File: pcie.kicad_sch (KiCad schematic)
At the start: 1 part, among them U1 MPFS250T-FCVG484

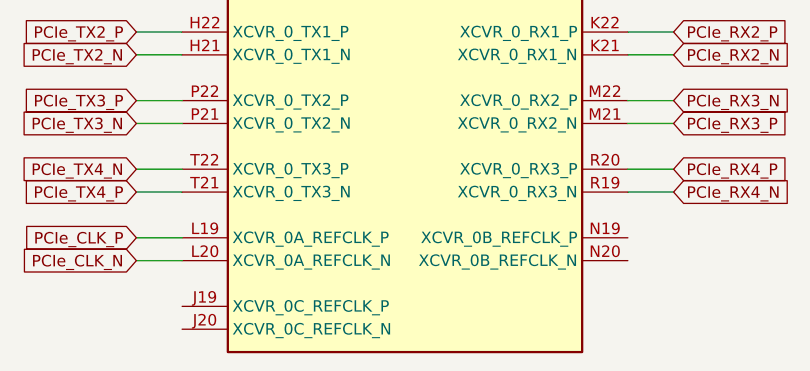
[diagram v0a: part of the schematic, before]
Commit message: [#54899] Flag not connected pins
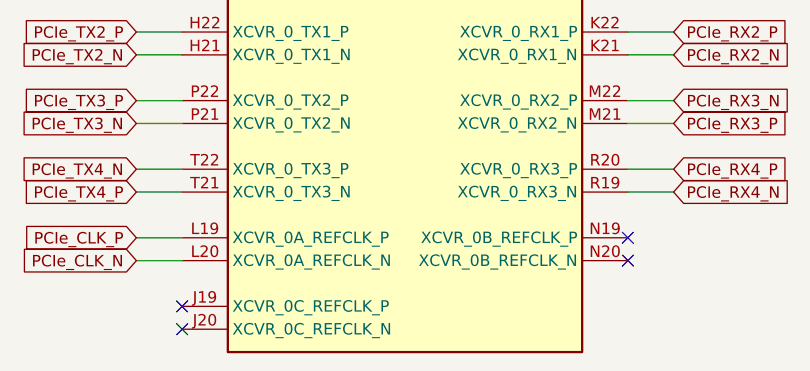
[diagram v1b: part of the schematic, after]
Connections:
- no-connect marks 0 -> 4
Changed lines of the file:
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@@
     (comment 1 "www.antmicro.com")
   )
+  (no_connect (at 177.8 158.75))
+  (no_connect (at 177.8 156.21))
+  (no_connect (at 227.33 148.59))
+  (no_connect (at 227.33 151.13))
   (wire (pts (xy 227.33 125.73) (xy 232.41 125.73))
     (stroke (width 0) (type default))

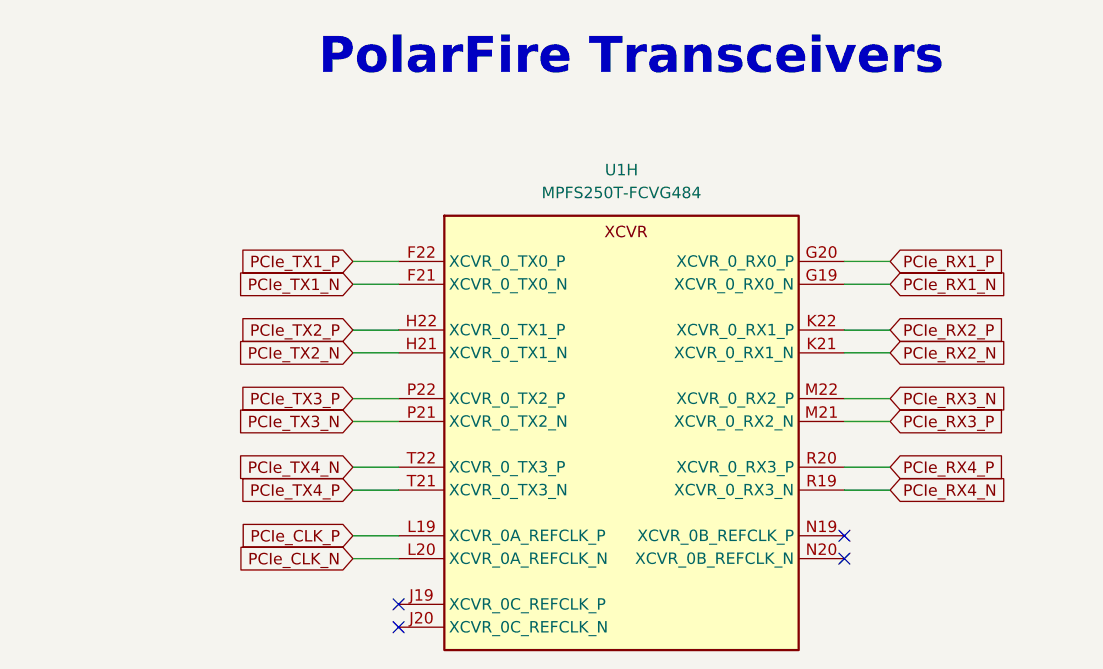
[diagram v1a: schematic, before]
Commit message: [#54899] Rename PCIe connections
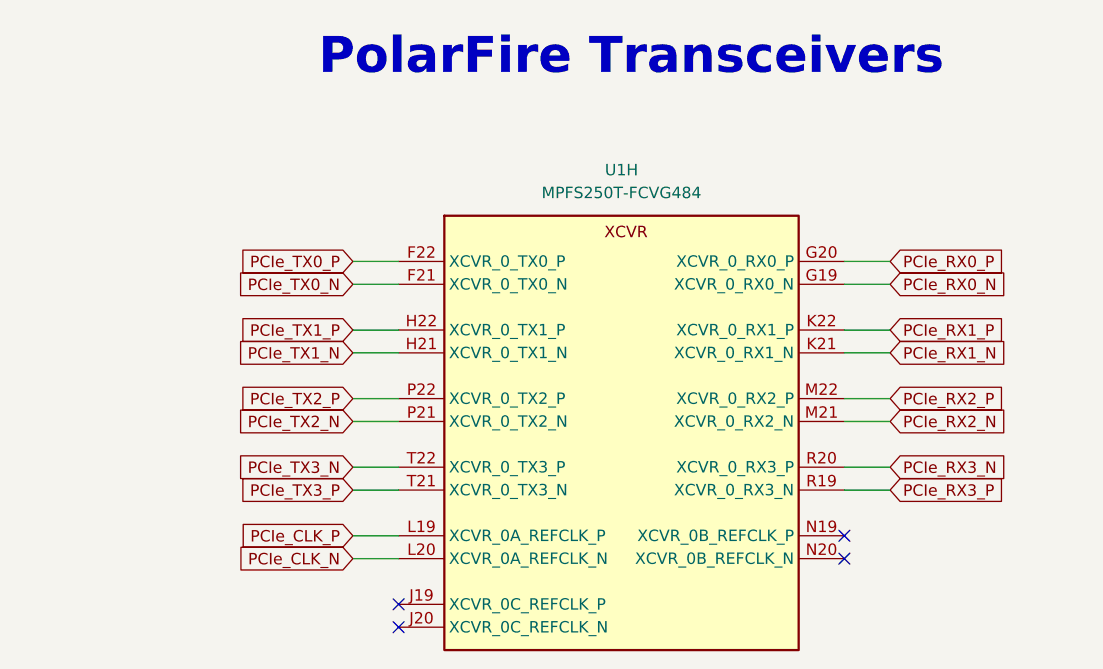
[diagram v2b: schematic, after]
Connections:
- net PCIe_RX4_N is gone; now on net PCIe_RX3_P: U1.R19 (XCVR_0_RX3_N)
- net PCIe_RX4_P is gone; now on net PCIe_RX3_N: U1.R20 (XCVR_0_RX3_P)
- net PCIe_TX4_N is gone; now on net PCIe_TX3_N: U1.T22 (XCVR_0_TX3_P)
- net PCIe_TX4_P is gone; now on net PCIe_TX3_P: U1.T21 (XCVR_0_TX3_N)
- net PCIe_RX1_N: now also U1.K21 (XCVR_0_RX1_N); no longer U1.G19 (XCVR_0_RX0_N)
- net PCIe_RX1_P: now also U1.K22 (XCVR_0_RX1_P); no longer U1.G20 (XCVR_0_RX0_P)
- net PCIe_RX2_N: now also U1.M21 (XCVR_0_RX2_N); no longer U1.K21 (XCVR_0_RX1_N)
- net PCIe_RX2_P: now also U1.M22 (XCVR_0_RX2_P); no longer U1.K22 (XCVR_0_RX1_P)
- net PCIe_RX3_N: no longer U1.M22 (XCVR_0_RX2_P)
- net PCIe_RX3_P: no longer U1.M21 (XCVR_0_RX2_N)
- net PCIe_TX1_N: now also U1.H21 (XCVR_0_TX1_N); no longer U1.F21 (XCVR_0_TX0_N)
- net PCIe_TX1_P: now also U1.H22 (XCVR_0_TX1_P); no longer U1.F22 (XCVR_0_TX0_P)
- net PCIe_TX2_N: now also U1.P21 (XCVR_0_TX2_N); no longer U1.H21 (XCVR_0_TX1_N)
- net PCIe_TX2_P: now also U1.P22 (XCVR_0_TX2_P); no longer U1.H22 (XCVR_0_TX1_P)
- net PCIe_TX3_N: no longer U1.P21 (XCVR_0_TX2_N)
- net PCIe_TX3_P: no longer U1.P22 (XCVR_0_TX2_P)
- new net PCIe_RX0_N: U1.G19 (XCVR_0_RX0_N)
- new net PCIe_RX0_P: U1.G20 (XCVR_0_RX0_P)
- new net PCIe_TX0_N: U1.F21 (XCVR_0_TX0_N)
- new net PCIe_TX0_P: U1.F22 (XCVR_0_TX0_P)
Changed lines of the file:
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@@
     (effects (font (size 4 4) (thickness 0.8) bold) (justify left bottom))
   )
-  (global_label "PCIe_TX4_N" (shape input) (at 172.72 140.97 180) (fields_autoplaced)
+  (global_label "PCIe_TX3_N" (shape input) (at 172.72 140.97 180) (fields_autoplaced)
     (effects (font (size 1.27 1.27)) (justify right))
-    (property "Intersheetrefs" "${INTERSHEET_REFS}" (at 159.4212 140.8906 0)
+    (property "Intersheetrefs" "${INTERSHEET_REFS}" (at 158.8491 140.97 0)
       (effects (font (size 1.27 1.27)) (justify right) hide)
     )
@@
     )
   )
-  (global_label "PCIe_TX1_N" (shape input) (at 172.72 120.65 180) (fields_autoplaced)
+  (global_label "PCIe_TX0_N" (shape input) (at 172.72 120.65 180) (fields_autoplaced)
     (effects (font (size 1.27 1.27)) (justify right))
-    (property "Intersheetrefs" "${INTERSHEET_REFS}" (at 159.4212 120.5706 0)
+    (property "Intersheetrefs" "${INTERSHEET_REFS}" (at 158.8491 120.65 0)
       (effects (font (size 1.27 1.27)) (justify right) hide)
     )
   )
-  (global_label "PCIe_TX3_P" (shape input) (at 172.72 133.35 180) (fields_autoplaced)
+  (global_label "PCIe_RX2_P" (shape input) (at 232.41 133.35 0) (fields_autoplaced)
+    (effects (font (size 1.27 1.27)) (justify left))
+    (property "Intersheetrefs" "${INTERSHEET_REFS}" (at 245.9507 133.2706 0)
+      (effects (font (size 1.27 1.27)) (justify left) hide)
+    )
+  )
+  (global_label "PCIe_TX2_P" (shape input) (at 172.72 133.35 180) (fields_autoplaced)
     (effects (font (size 1.27 1.27)) (justify right))
-    (property "Intersheetrefs" "${INTERSHEET_REFS}" (at 159.4817 133.2706 0)
+    (property "Intersheetrefs" "${INTERSHEET_REFS}" (at 158.9096 133.35 0)
       (effects (font (size 1.27 1.27)) (justify right) hide)
     )
   )
-  (global_label "PCIe_RX2_N" (shape input) (at 232.41 128.27 0) (fields_autoplaced)
+  (global_label "PCIe_RX0_N" (shape input) (at 232.41 120.65 0) (fields_autoplaced)
     (effects (font (size 1.27 1.27)) (justify left))
-    (property "Intersheetrefs" "${INTERSHEET_REFS}" (at 246.0112 128.1906 0)
+    (property "Intersheetrefs" "${INTERSHEET_REFS}" (at 246.5833 120.65 0)
       (effects (font (size 1.27 1.27)) (justify left) hide)
     )
   )
-  (global_label "PCIe_RX1_N" (shape input) (at 232.41 120.65 0) (fields_autoplaced)
+  (global_label "PCIe_TX2_N" (shape input) (at 172.72 135.89 180) (fields_autoplaced)
+    (effects (font (size 1.27 1.27)) (justify right))
+    (property "Intersheetrefs" "${INTERSHEET_REFS}" (at 158.8491 135.89 0)
+      (effects (font (size 1.27 1.27)) (justify right) hide)
+    )
+  )
+  (global_label "PCIe_RX3_N" (shape input) (at 232.41 140.97 0) (fields_autoplaced)
     (effects (font (size 1.27 1.27)) (justify left))
-    (property "Intersheetrefs" "${INTERSHEET_REFS}" (at 246.0112 120.5706 0)
+    (property "Intersheetrefs" "${INTERSHEET_REFS}" (at 246.0112 140.8906 0)
       (effects (font (size 1.27 1.27)) (justify left) hide)
     )
   )
-  (global_label "PCIe_TX3_N" (shape input) (at 172.72 135.89 180) (fields_autoplaced)
+  (global_label "PCIe_TX3_P" (shape input) (at 172.72 143.51 180) (fields_autoplaced)
     (effects (font (size 1.27 1.27)) (justify right))
-    (property "Intersheetrefs" "${INTERSHEET_REFS}" (at 159.4212 135.8106 0)
+    (property "Intersheetrefs" "${INTERSHEET_REFS}" (at 158.9096 143.51 0)
       (effects (font (size 1.27 1.27)) (justify right) hide)
     )
   )
-  (global_label "PCIe_TX4_P" (shape input) (at 172.72 143.51 180) (fields_autoplaced)
+  (global_label "PCIe_TX1_N" (shape input) (at 172.72 128.27 180) (fields_autoplaced)
     (effects (font (size 1.27 1.27)) (justify right))
-    (property "Intersheetrefs" "${INTERSHEET_REFS}" (at 159.4817 143.4306 0)
+    (property "Intersheetrefs" "${INTERSHEET_REFS}" (at 158.8491 128.27 0)
       (effects (font (size 1.27 1.27)) (justify right) hide)
     )
   )
-  (global_label "PCIe_TX2_N" (shape input) (at 172.72 128.27 180) (fields_autoplaced)
+  (global_label "PCIe_TX0_P" (shape input) (at 172.72 118.11 180) (fields_autoplaced)
     (effects (font (size 1.27 1.27)) (justify right))
-    (property "Intersheetrefs" "${INTERSHEET_REFS}" (at 159.4212 128.1906 0)
+    (property "Intersheetrefs" "${INTERSHEET_REFS}" (at 158.9096 118.11 0)
       (effects (font (size 1.27 1.27)) (justify right) hide)
     )
   )
-  (global_label "PCIe_TX1_P" (shape input) (at 172.72 118.11 180) (fields_autoplaced)
+  (global_label "PCIe_RX1_P" (shape input) (at 232.41 125.73 0) (fields_autoplaced)
+    (effects (font (size 1.27 1.27)) (justify left))
+    (property "Intersheetrefs" "${INTERSHEET_REFS}" (at 246.5228 125.73 0)
+      (effects (font (size 1.27 1.27)) (justify left) hide)
+    )
+  )
+  (global_label "PCIe_TX1_P" (shape input) (at 172.72 125.73 180) (fields_autoplaced)
     (effects (font (size 1.27 1.27)) (justify right))
-    (property "Intersheetrefs" "${INTERSHEET_REFS}" (at 159.4817 118.0306 0)
+    (property "Intersheetrefs" "${INTERSHEET_REFS}" (at 158.9096 125.73 0)
       (effects (font (size 1.27 1.27)) (justify right) hide)
     )
   )
-  (global_label "PCIe_TX2_P" (shape input) (at 172.72 125.73 180) (fields_autoplaced)
-    (effects (font (size 1.27 1.27)) (justify right))
-    (property "Intersheetrefs" "${INTERSHEET_REFS}" (at 159.4817 125.6506 0)
-      (effects (font (size 1.27 1.27)) (justify right) hide)
-    )
-  )
-  (global_label "PCIe_RX3_P" (shape input) (at 232.41 135.89 0) (fields_autoplaced)
+  (global_label "PCIe_RX3_P" (shape input) (at 232.41 143.51 0) (fields_autoplaced)
     (effects (font (size 1.27 1.27)) (justify left))
-    (property "Intersheetrefs" "${INTERSHEET_REFS}" (at 245.9507 135.8106 0)
+    (property "Intersheetrefs" "${INTERSHEET_REFS}" (at 245.9507 143.4306 0)
       (effects (font (size 1.27 1.27)) (justify left) hide)
     )
   )
-  (global_label "PCIe_RX2_P" (shape input) (at 232.41 125.73 0) (fields_autoplaced)
+  (global_label "PCIe_RX2_N" (shape input) (at 232.41 135.89 0) (fields_autoplaced)
     (effects (font (size 1.27 1.27)) (justify left))
-    (property "Intersheetrefs" "${INTERSHEET_REFS}" (at 245.9507 125.6506 0)
+    (property "Intersheetrefs" "${INTERSHEET_REFS}" (at 246.0112 135.8106 0)
       (effects (font (size 1.27 1.27)) (justify left) hide)
     )
   )
-  (global_label "PCIe_RX3_N" (shape input) (at 232.41 133.35 0) (fields_autoplaced)
+  (global_label "PCIe_RX1_N" (shape input) (at 232.41 128.27 0) (fields_autoplaced)
     (effects (font (size 1.27 1.27)) (justify left))
-    (property "Intersheetrefs" "${INTERSHEET_REFS}" (at 246.0112 133.2706 0)
-      (effects (font (size 1.27 1.27)) (justify left) hide)
-    )
-  )
-  (global_label "PCIe_RX4_P" (shape input) (at 232.41 140.97 0) (fields_autoplaced)
-    (effects (font (size 1.27 1.27)) (justify left))
-    (property "Intersheetrefs" "${INTERSHEET_REFS}" (at 245.9507 140.8906 0)
+    (property "Intersheetrefs" "${INTERSHEET_REFS}" (at 246.5833 128.27 0)
       (effects (font (size 1.27 1.27)) (justify left) hide)
     )
@@
     )
   )
-  (global_label "PCIe_RX1_P" (shape input) (at 232.41 118.11 0) (fields_autoplaced)
+  (global_label "PCIe_RX0_P" (shape input) (at 232.41 118.11 0) (fields_autoplaced)
     (effects (font (size 1.27 1.27)) (justify left))
-    (property "Intersheetrefs" "${INTERSHEET_REFS}" (at 245.9507 118.0306 0)
+    (property "Intersheetrefs" "${INTERSHEET_REFS}" (at 246.5228 118.11 0)
       (effects (font (size 1.27 1.27)) (justify left) hide)
     )
-  )
-  (global_label "PCIe_RX4_N" (shape input) (at 232.41 143.51 0) (fields_autoplaced)
-    (effects (font (size 1.27 1.27)) (justify left))
-    (property "Intersheetrefs" "${INTERSHEET_REFS}" (at 246.0112 143.4306 0)
-      (effects (font (size 1.27 1.27)) (justify left) hide)
-    )

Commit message: [#54899] Update symbols
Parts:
- U1: footprint antmicro-footprints:BGA-484_19x19mm_Layout22x22_P0.8mm_FCVG484 -> antmicro-footprints:BGA-484_19x19mm_Layout22x22_P0.8mm_MPFS250T-FCVG484
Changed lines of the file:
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@@
       (effects (font (size 1.27 1.27) (thickness 0.15)) (justify left bottom) hide)
     )
-    (property "Footprint" "antmicro-footprints:BGA-484_19x19mm_Layout22x22_P0.8mm_FCVG484" (at 281.94 128.27 0)
+    (property "Footprint" "antmicro-footprints:BGA-484_19x19mm_Layout22x22_P0.8mm_MPFS250T-FCVG484" (at 281.94 128.27 0)
       (effects (font (size 1.27 1.27) (thickness 0.15)) (justify left bottom) hide)
     )

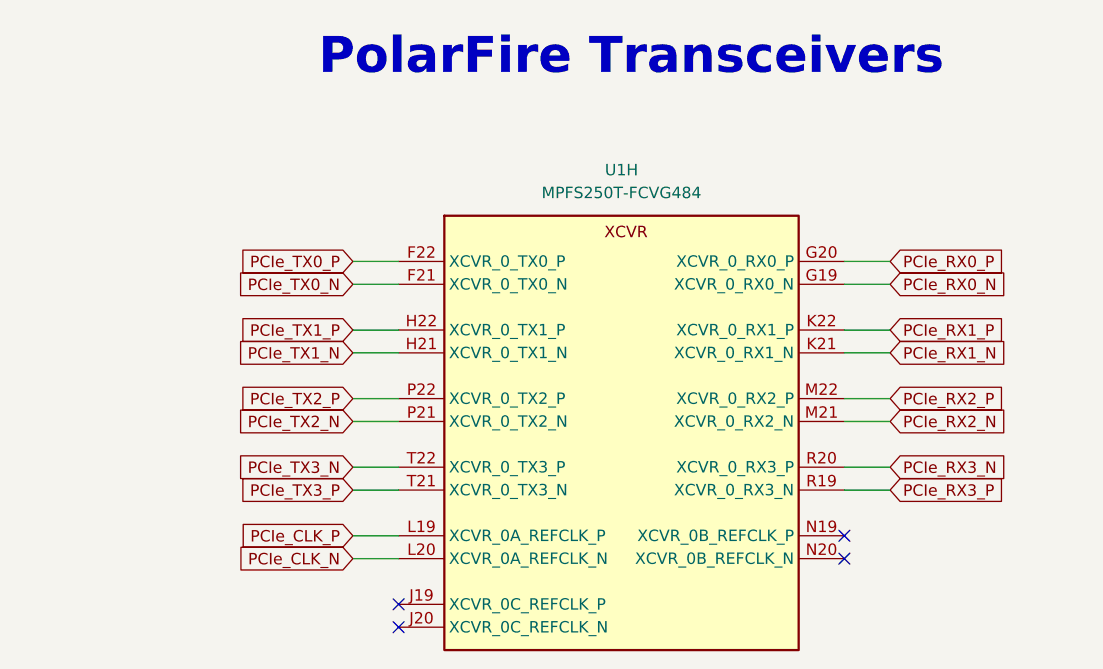
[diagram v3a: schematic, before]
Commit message: [#55288] Add 100nF capacitors on PCIe TX lanes
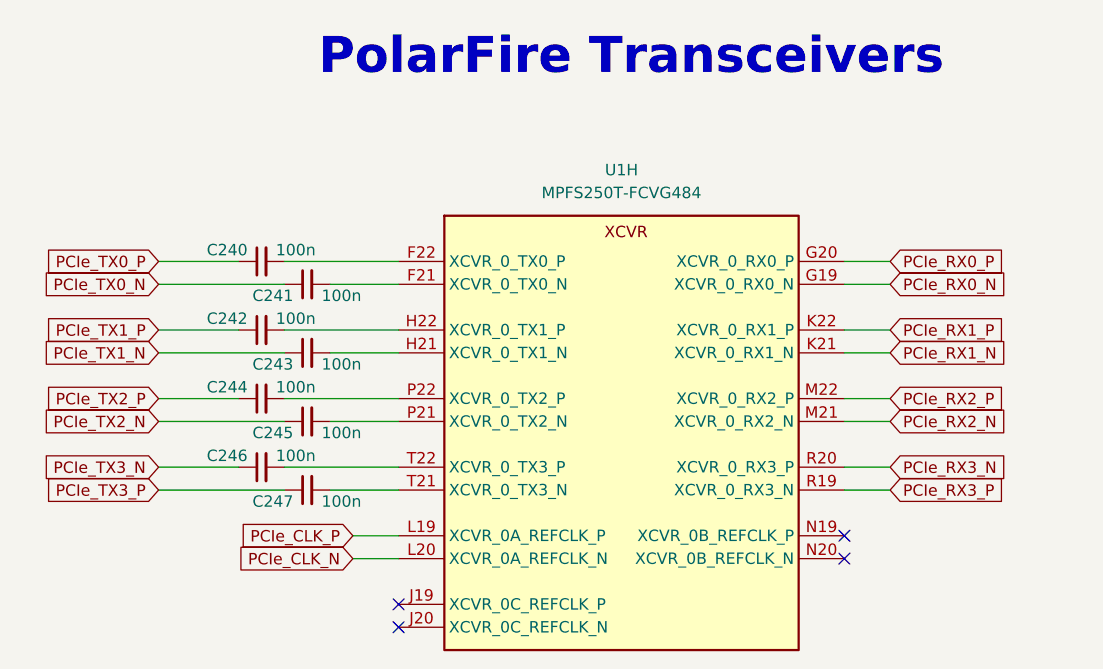
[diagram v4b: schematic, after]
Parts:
- added C240, C241, C242, C243, C244, C245, C246, C247: C_100n_0201_25V, antmicro-footprints:C_0201, symbol antmicroCapacitorsmisc:C_100n_0201_25V
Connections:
- net PCIe_TX0_N: now also C241.1; no longer U1.F21 (XCVR_0_TX0_N)
- net PCIe_TX0_P: now also C240.1; no longer U1.F22 (XCVR_0_TX0_P)
- net PCIe_TX1_N: now also C243.1; no longer U1.H21 (XCVR_0_TX1_N)
- net PCIe_TX1_P: now also C242.1; no longer U1.H22 (XCVR_0_TX1_P)
- net PCIe_TX2_N: now also C245.1; no longer U1.P21 (XCVR_0_TX2_N)
- net PCIe_TX2_P: now also C244.1; no longer U1.P22 (XCVR_0_TX2_P)
- net PCIe_TX3_N: now also C246.1; no longer U1.T22 (XCVR_0_TX3_P)
- net PCIe_TX3_P: now also C247.1; no longer U1.T21 (XCVR_0_TX3_N)
- new net: C247.2, U1.T21 (XCVR_0_TX3_N)
- new net: C242.2, U1.H22 (XCVR_0_TX1_P)
- new net: C245.2, U1.P21 (XCVR_0_TX2_N)
- new net: C243.2, U1.H21 (XCVR_0_TX1_N)
- new net: C240.2, U1.F22 (XCVR_0_TX0_P)
- new net: C241.2, U1.F21 (XCVR_0_TX0_N)
- new net: C246.2, U1.T22 (XCVR_0_TX3_P)
- new net: C244.2, U1.P22 (XCVR_0_TX2_P)
